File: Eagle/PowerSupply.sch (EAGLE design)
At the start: 9 parts, among them IC1 7812T, X1 MKDSN1,5/3-5,08

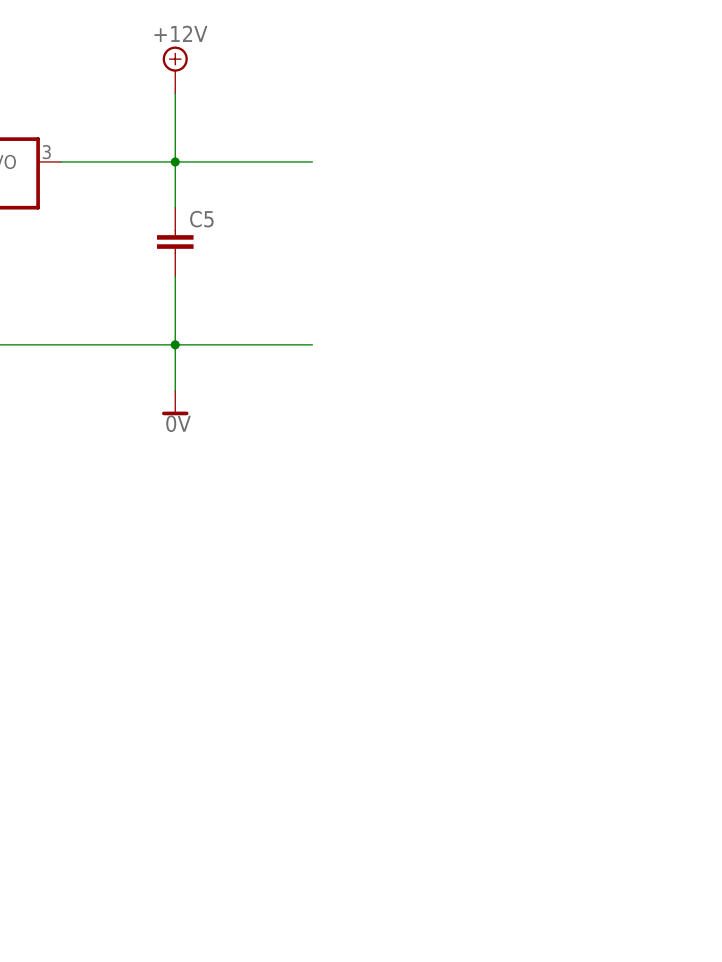
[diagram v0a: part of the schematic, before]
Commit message: - CPUBoard:   - another pin-header added for RS-485 UART   - correct termination for RS-485 A/B lines - PowerSupply: terminals added - eagle_clean.sh: remove backup files of Eagle
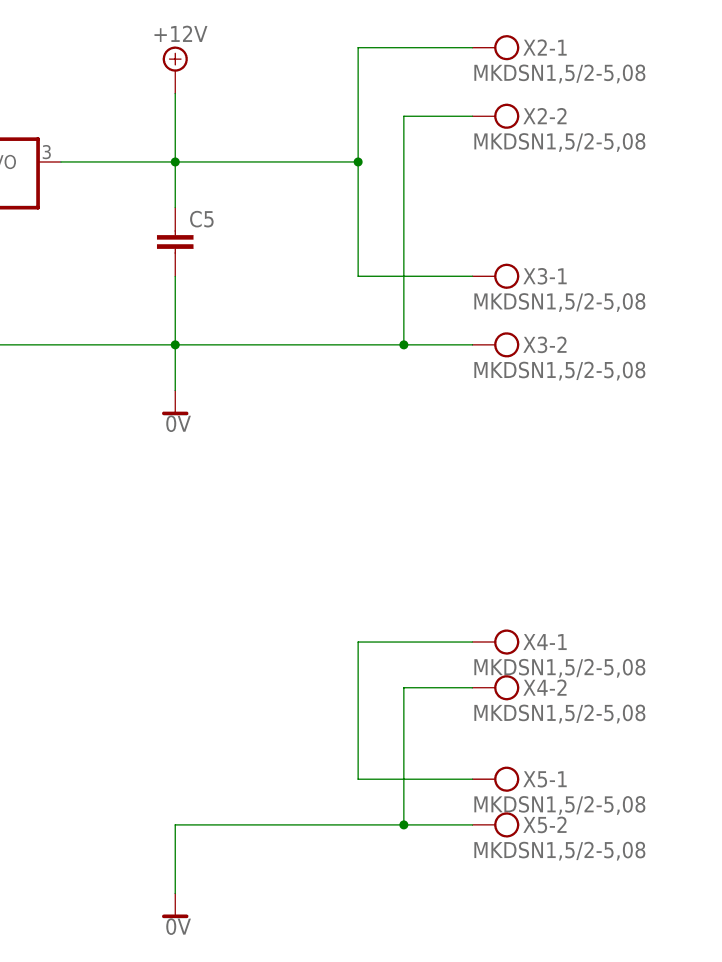
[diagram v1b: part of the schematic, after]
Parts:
- added X2, X3, X4, X5: MKDSN1,5/2-5,08, con-phoenix-508:MKDSN1,5/2-5,08
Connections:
- new net N$9: X4-1.KL, X5-1.KL
- net +12V: now also X2-1.KL, X3-1.KL
- net 0V: now also X2-2.KL, X3-2.KL, X4-2.KL, X5-2.KL
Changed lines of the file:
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@@
 <part name="SUPPLY2" library="supply2" deviceset="+12V" device=""/>
 <part name="SUPPLY3" library="supply2" deviceset="0V" device=""/>
+<part name="X2" library="con-phoenix-508" deviceset="MKDSN1,5/2-5,08" device=""/>
+<part name="X3" library="con-phoenix-508" deviceset="MKDSN1,5/2-5,08" device=""/>
+<part name="X4" library="con-phoenix-508" deviceset="MKDSN1,5/2-5,08" device=""/>
+<part name="X5" library="con-phoenix-508" deviceset="MKDSN1,5/2-5,08" device=""/>
+<part name="SUPPLY4" library="supply2" deviceset="0V" device=""/>
 </parts>
 <sheets>
@@
 <instance part="SUPPLY2" gate="+12V" x="195.58" y="160.02"/>
 <instance part="SUPPLY3" gate="0V" x="195.58" y="121.92"/>
+<instance part="X2" gate="-1" x="231.14" y="162.56"/>
+<instance part="X2" gate="-2" x="231.14" y="154.94"/>
+<instance part="X3" gate="-1" x="231.14" y="137.16"/>
+<instance part="X3" gate="-2" x="231.14" y="129.54"/>
+<instance part="X4" gate="-1" x="231.14" y="96.52"/>
+<instance part="X4" gate="-2" x="231.14" y="91.44"/>
+<instance part="X5" gate="-1" x="231.14" y="81.28"/>
+<instance part="X5" gate="-2" x="231.14" y="76.2"/>
+<instance part="SUPPLY4" gate="0V" x="195.58" y="66.04"/>
 </instances>
 <busses>
@@
 <wire x1="195.58" y1="149.86" x2="195.58" y2="157.48" width="0.1524" layer="91"/>
 <junction x="195.58" y="149.86"/>
-<wire x1="195.58" y1="149.86" x2="210.82" y2="149.86" width="0.1524" layer="91"/>
+<wire x1="195.58" y1="149.86" x2="215.9" y2="149.86" width="0.1524" layer="91"/>
+<pinref part="X2" gate="-1" pin="KL"/>
+<wire x1="228.6" y1="162.56" x2="215.9" y2="162.56" width="0.1524" layer="91"/>
+<wire x1="215.9" y1="162.56" x2="215.9" y2="149.86" width="0.1524" layer="91"/>
+<wire x1="215.9" y1="149.86" x2="215.9" y2="137.16" width="0.1524" layer="91"/>
+<junction x="215.9" y="149.86"/>
+<pinref part="X3" gate="-1" pin="KL"/>
+<wire x1="215.9" y1="137.16" x2="228.6" y2="137.16" width="0.1524" layer="91"/>
 </segment>
 </net>
@@
 <wire x1="195.58" y1="124.46" x2="195.58" y2="129.54" width="0.1524" layer="91"/>
 <junction x="195.58" y="129.54"/>
-<wire x1="195.58" y1="129.54" x2="210.82" y2="129.54" width="0.1524" layer="91"/>
 <pinref part="IC1" gate="A1" pin="GND"/>
 <wire x1="172.72" y1="142.24" x2="172.72" y2="129.54" width="0.1524" layer="91"/>
 <junction x="172.72" y="129.54"/>
+<pinref part="X3" gate="-2" pin="KL"/>
+<wire x1="228.6" y1="129.54" x2="220.98" y2="129.54" width="0.1524" layer="91"/>
+<pinref part="X2" gate="-2" pin="KL"/>
+<wire x1="220.98" y1="129.54" x2="195.58" y2="129.54" width="0.1524" layer="91"/>
+<wire x1="228.6" y1="154.94" x2="220.98" y2="154.94" width="0.1524" layer="91"/>
+<wire x1="220.98" y1="154.94" x2="220.98" y2="129.54" width="0.1524" layer="91"/>
+<junction x="220.98" y="129.54"/>
+</segment>
+<segment>
+<pinref part="SUPPLY4" gate="0V" pin="0V"/>
+<wire x1="195.58" y1="68.58" x2="195.58" y2="76.2" width="0.1524" layer="91"/>
+<pinref part="X5" gate="-2" pin="KL"/>
+<wire x1="195.58" y1="76.2" x2="220.98" y2="76.2" width="0.1524" layer="91"/>
+<wire x1="220.98" y1="76.2" x2="228.6" y2="76.2" width="0.1524" layer="91"/>
+<wire x1="220.98" y1="76.2" x2="220.98" y2="91.44" width="0.1524" layer="91"/>
+<junction x="220.98" y="76.2"/>
+<pinref part="X4" gate="-2" pin="KL"/>
+<wire x1="220.98" y1="91.44" x2="228.6" y2="91.44" width="0.1524" layer="91"/>
 </segment>
 </net>
+<net name="N$9" class="0">
+<segment>
+<pinref part="X5" gate="-1" pin="KL"/>
+<wire x1="228.6" y1="81.28" x2="215.9" y2="81.28" width="0.1524" layer="91"/>
+<wire x1="215.9" y1="81.28" x2="215.9" y2="96.52" width="0.1524" layer="91"/>
+<pinref part="X4" gate="-1" pin="KL"/>
+<wire x1="215.9" y1="96.52" x2="228.6" y2="96.52" width="0.1524" layer="91"/>
+</segment>
+</net>

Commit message: - small corrections
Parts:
- C1, C2: value (none) -> 2200u
- C4, C5: value (none) -> 100n
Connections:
- removed net N$9: X4-1.KL, X5-1.KL
- new net N$7: X4-1.KL, X4-2.KL
- net +12V: now also X2-2.KL; no longer X3-1.KL
- net 0V: now also X3-1.KL, X5-1.KL; no longer X2-2.KL, X4-2.KL
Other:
- moved on the sheet: X2-1, X2-2
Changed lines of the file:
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@@
 </classes>
 <parts>
-<part name="FRAME1" library="frames" deviceset="DINA4_L" device=""/>
+<part name="FRAME1" library="frames" deviceset="DINA4_L" device="" value="PowerSupply"/>
 <part name="IC1" library="linear" deviceset="78*" device="T" technology="12"/>
 <part name="B1" library="rectifier" deviceset="B-DIL" device="" value="B80C800"/>
-<part name="C1" library="rcl" deviceset="CPOL-EU" device="E55-30AXIAL"/>
-<part name="C2" library="rcl" deviceset="CPOL-EU" device="E55-30AXIAL"/>
-<part name="C4" library="rcl" deviceset="C-EU" device="050-024X044"/>
-<part name="C5" library="rcl" deviceset="C-EU" device="050-024X044"/>
+<part name="C1" library="rcl" deviceset="CPOL-EU" device="E55-30AXIAL" value="2200u"/>
+<part name="C2" library="rcl" deviceset="CPOL-EU" device="E55-30AXIAL" value="2200u"/>
+<part name="C4" library="rcl" deviceset="C-EU" device="050-024X044" value="100n"/>
+<part name="C5" library="rcl" deviceset="C-EU" device="050-024X044" value="100n"/>
 <part name="F1" library="fuse" deviceset="FUSE" device="SHK20L"/>
 <part name="X1" library="con-phoenix-508" deviceset="MKDSN1,5/3-5,08" device=""/>
@@
 <instance part="SUPPLY2" gate="+12V" x="195.58" y="160.02"/>
 <instance part="SUPPLY3" gate="0V" x="195.58" y="121.92"/>
-<instance part="X2" gate="-1" x="231.14" y="162.56"/>
-<instance part="X2" gate="-2" x="231.14" y="154.94"/>
+<instance part="X2" gate="-1" x="231.14" y="157.48"/>
+<instance part="X2" gate="-2" x="231.14" y="149.86"/>
 <instance part="X3" gate="-1" x="231.14" y="137.16"/>
 <instance part="X3" gate="-2" x="231.14" y="129.54"/>
@@
 <wire x1="195.58" y1="149.86" x2="215.9" y2="149.86" width="0.1524" layer="91"/>
 <pinref part="X2" gate="-1" pin="KL"/>
-<wire x1="228.6" y1="162.56" x2="215.9" y2="162.56" width="0.1524" layer="91"/>
-<wire x1="215.9" y1="162.56" x2="215.9" y2="149.86" width="0.1524" layer="91"/>
-<wire x1="215.9" y1="149.86" x2="215.9" y2="137.16" width="0.1524" layer="91"/>
+<wire x1="228.6" y1="157.48" x2="215.9" y2="157.48" width="0.1524" layer="91"/>
+<wire x1="215.9" y1="157.48" x2="215.9" y2="149.86" width="0.1524" layer="91"/>
+<pinref part="X2" gate="-2" pin="KL"/>
+<wire x1="228.6" y1="149.86" x2="215.9" y2="149.86" width="0.1524" layer="91"/>
 <junction x="215.9" y="149.86"/>
-<pinref part="X3" gate="-1" pin="KL"/>
-<wire x1="215.9" y1="137.16" x2="228.6" y2="137.16" width="0.1524" layer="91"/>
 </segment>
 </net>
@@
 <junction x="172.72" y="129.54"/>
 <pinref part="X3" gate="-2" pin="KL"/>
-<wire x1="228.6" y1="129.54" x2="220.98" y2="129.54" width="0.1524" layer="91"/>
-<pinref part="X2" gate="-2" pin="KL"/>
-<wire x1="220.98" y1="129.54" x2="195.58" y2="129.54" width="0.1524" layer="91"/>
-<wire x1="228.6" y1="154.94" x2="220.98" y2="154.94" width="0.1524" layer="91"/>
-<wire x1="220.98" y1="154.94" x2="220.98" y2="129.54" width="0.1524" layer="91"/>
-<junction x="220.98" y="129.54"/>
+<wire x1="228.6" y1="129.54" x2="215.9" y2="129.54" width="0.1524" layer="91"/>
+<pinref part="X3" gate="-1" pin="KL"/>
+<wire x1="215.9" y1="129.54" x2="195.58" y2="129.54" width="0.1524" layer="91"/>
+<wire x1="228.6" y1="137.16" x2="215.9" y2="137.16" width="0.1524" layer="91"/>
+<wire x1="215.9" y1="137.16" x2="215.9" y2="129.54" width="0.1524" layer="91"/>
+<junction x="215.9" y="129.54"/>
 </segment>
 <segment>
@@
 <wire x1="195.58" y1="68.58" x2="195.58" y2="76.2" width="0.1524" layer="91"/>
 <pinref part="X5" gate="-2" pin="KL"/>
-<wire x1="195.58" y1="76.2" x2="220.98" y2="76.2" width="0.1524" layer="91"/>
-<wire x1="220.98" y1="76.2" x2="228.6" y2="76.2" width="0.1524" layer="91"/>
-<wire x1="220.98" y1="76.2" x2="220.98" y2="91.44" width="0.1524" layer="91"/>
-<junction x="220.98" y="76.2"/>
+<wire x1="195.58" y1="76.2" x2="215.9" y2="76.2" width="0.1524" layer="91"/>
+<pinref part="X5" gate="-1" pin="KL"/>
+<wire x1="215.9" y1="76.2" x2="228.6" y2="76.2" width="0.1524" layer="91"/>
+<wire x1="228.6" y1="81.28" x2="215.9" y2="81.28" width="0.1524" layer="91"/>
+<wire x1="215.9" y1="81.28" x2="215.9" y2="76.2" width="0.1524" layer="91"/>
+<junction x="215.9" y="76.2"/>
+</segment>
+</net>
+<net name="N$7" class="0">
+<segment>
 <pinref part="X4" gate="-2" pin="KL"/>
-<wire x1="220.98" y1="91.44" x2="228.6" y2="91.44" width="0.1524" layer="91"/>
-</segment>
-</net>
-<net name="N$9" class="0">
-<segment>
-<pinref part="X5" gate="-1" pin="KL"/>
-<wire x1="228.6" y1="81.28" x2="215.9" y2="81.28" width="0.1524" layer="91"/>
-<wire x1="215.9" y1="81.28" x2="215.9" y2="96.52" width="0.1524" layer="91"/>
+<wire x1="215.9" y1="91.44" x2="228.6" y2="91.44" width="0.1524" layer="91"/>
 <pinref part="X4" gate="-1" pin="KL"/>
 <wire x1="215.9" y1="96.52" x2="228.6" y2="96.52" width="0.1524" layer="91"/>
+<wire x1="215.9" y1="91.44" x2="215.9" y2="96.52" width="0.1524" layer="91"/>
 </segment>
 </net>
@@
 </sheet>
 </sheets>
+<errors>
+</errors>
 </schematic>
 </drawing>

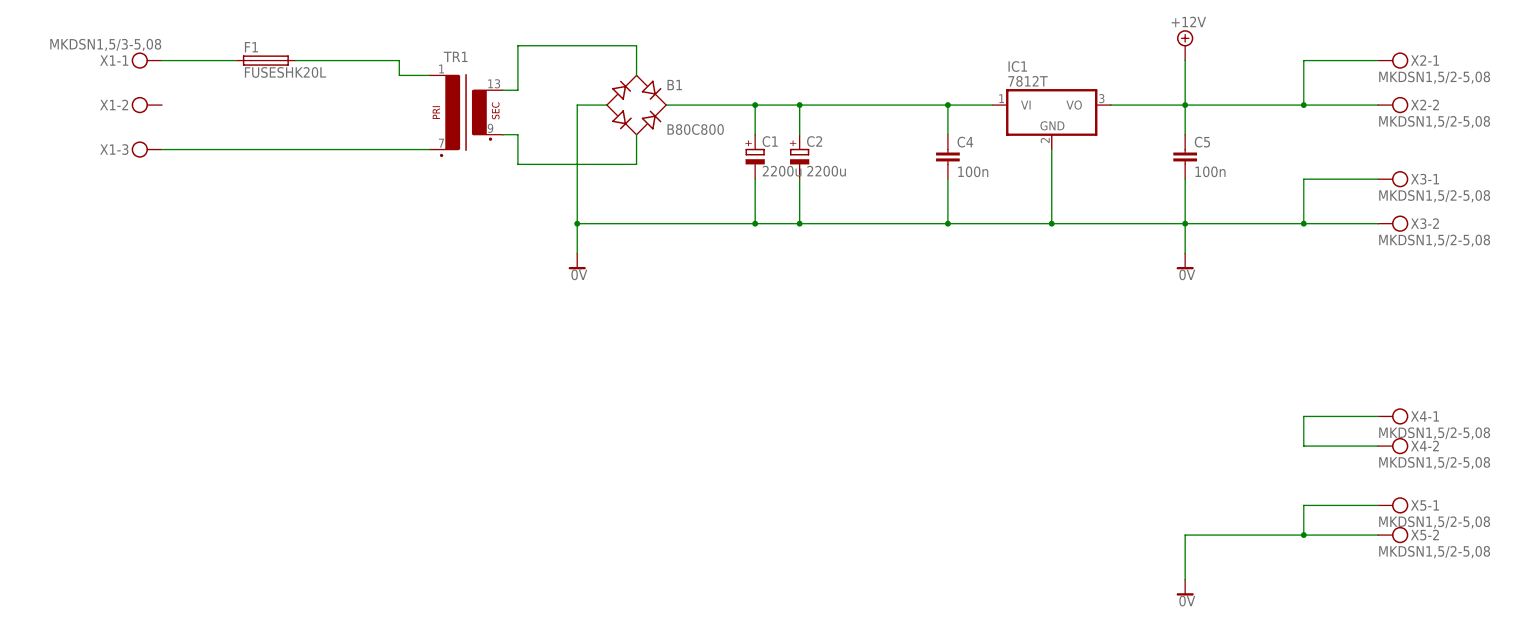
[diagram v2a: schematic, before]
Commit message: - PowerSupply: schematic continued, proposal for board layout
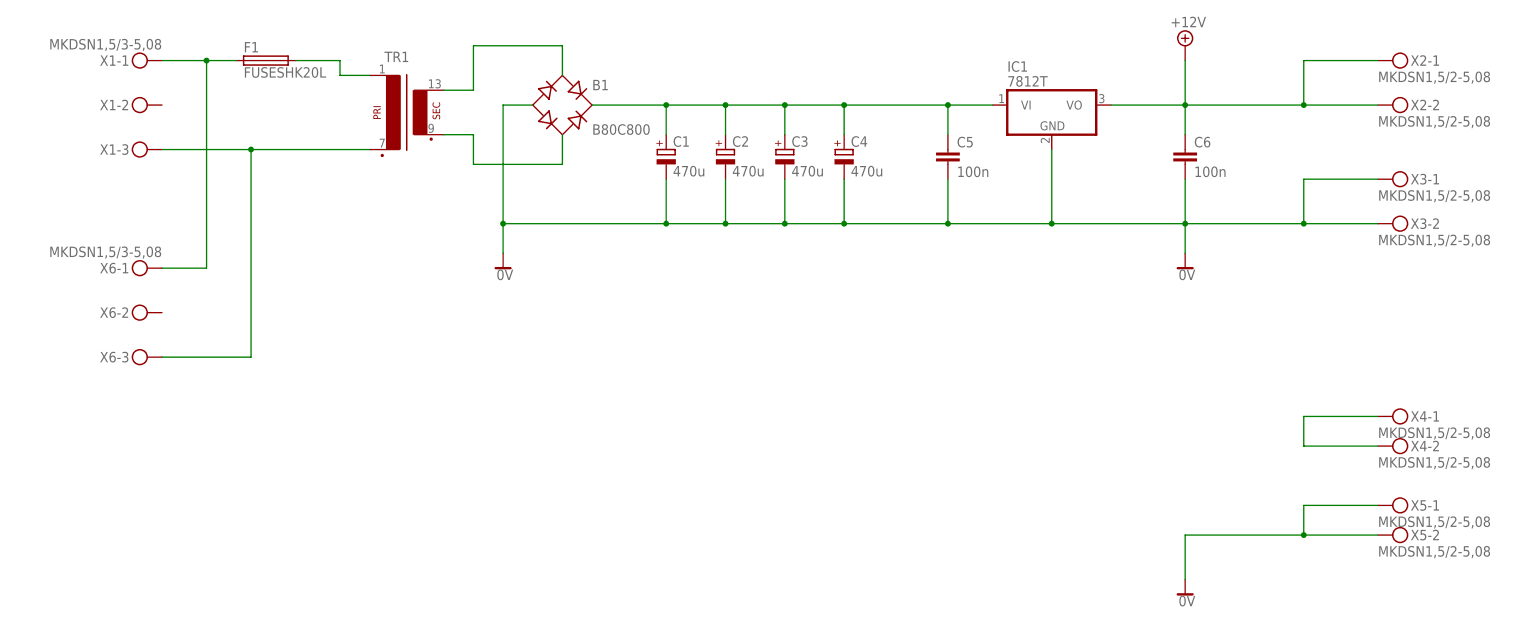
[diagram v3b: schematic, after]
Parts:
- added C3: 470u, rcl:CPOL-EUE5-10.5
- added C6: 100n, rcl:C-EU050-024X044
- added X6: MKDSN1,5/3-5,08, con-phoenix-508:MKDSN1,5/3-5,08
- C1, C2: value 2200u -> 470u; device rcl:CPOL-EUE55-30AXIAL -> rcl:CPOL-EUE5-10.5
- C4: value 100n -> 470u; device rcl:C-EU050-024X044 -> rcl:CPOL-EUE5-10.5
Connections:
- net +12V: now also C6.1; no longer C5.1
- net 0V: now also C3.-, C4.-, C6.2; no longer C4.2
- net N$1: now also X6-1.KL
- net N$3: now also X6-3.KL
- net N$6: now also C3.+, C4.+, C5.1; no longer C4.1
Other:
- moved on the sheet: B1, C1, C2, C5, TR1

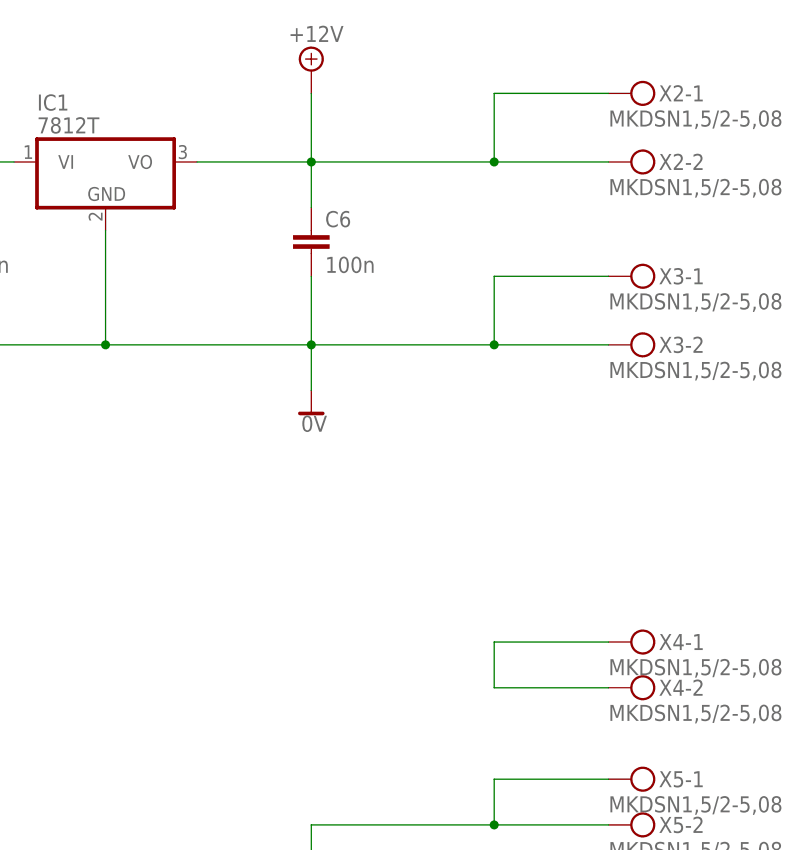
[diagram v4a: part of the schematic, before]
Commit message: - fixed some error, re-routing done
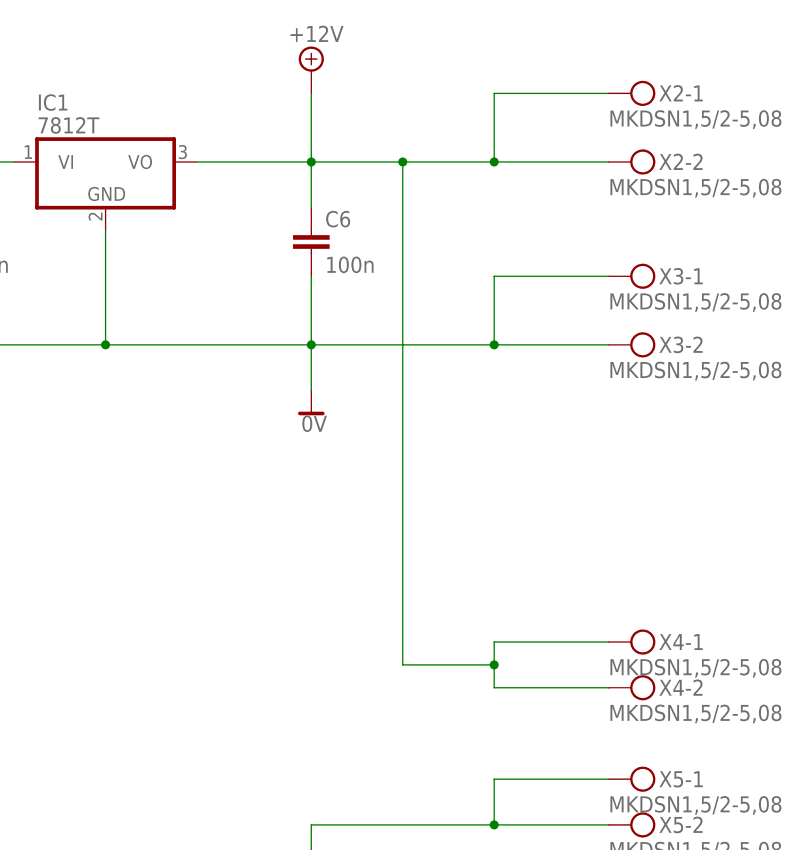
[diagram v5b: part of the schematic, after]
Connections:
- removed net N$7: X4-1.KL, X4-2.KL
- net +12V: now also X4-1.KL, X4-2.KL
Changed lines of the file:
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@@
 <wire x1="195.58" y1="149.86" x2="195.58" y2="157.48" width="0.1524" layer="91"/>
 <junction x="195.58" y="149.86"/>
-<wire x1="195.58" y1="149.86" x2="215.9" y2="149.86" width="0.1524" layer="91"/>
+<wire x1="195.58" y1="149.86" x2="205.74" y2="149.86" width="0.1524" layer="91"/>
 <pinref part="X2" gate="-1" pin="KL"/>
+<wire x1="205.74" y1="149.86" x2="215.9" y2="149.86" width="0.1524" layer="91"/>
 <wire x1="228.6" y1="157.48" x2="215.9" y2="157.48" width="0.1524" layer="91"/>
 <wire x1="215.9" y1="157.48" x2="215.9" y2="149.86" width="0.1524" layer="91"/>
@@
 <wire x1="228.6" y1="149.86" x2="215.9" y2="149.86" width="0.1524" layer="91"/>
 <junction x="215.9" y="149.86"/>
+<wire x1="205.74" y1="149.86" x2="205.74" y2="93.98" width="0.1524" layer="91"/>
+<junction x="205.74" y="149.86"/>
+<pinref part="X4" gate="-1" pin="KL"/>
+<wire x1="215.9" y1="96.52" x2="228.6" y2="96.52" width="0.1524" layer="91"/>
+<pinref part="X4" gate="-2" pin="KL"/>
+<wire x1="215.9" y1="91.44" x2="228.6" y2="91.44" width="0.1524" layer="91"/>
+<wire x1="215.9" y1="91.44" x2="215.9" y2="93.98" width="0.1524" layer="91"/>
+<wire x1="215.9" y1="93.98" x2="215.9" y2="96.52" width="0.1524" layer="91"/>
+<wire x1="205.74" y1="93.98" x2="215.9" y2="93.98" width="0.1524" layer="91"/>
+<junction x="215.9" y="93.98"/>
 </segment>
 </net>
@@
 </segment>
 </net>
-<net name="N$7" class="0">
-<segment>
-<pinref part="X4" gate="-2" pin="KL"/>
-<wire x1="215.9" y1="91.44" x2="228.6" y2="91.44" width="0.1524" layer="91"/>
-<pinref part="X4" gate="-1" pin="KL"/>
-<wire x1="215.9" y1="96.52" x2="228.6" y2="96.52" width="0.1524" layer="91"/>
-<wire x1="215.9" y1="91.44" x2="215.9" y2="96.52" width="0.1524" layer="91"/>
-</segment>
-</net>
